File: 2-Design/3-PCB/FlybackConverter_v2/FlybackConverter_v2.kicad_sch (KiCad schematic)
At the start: 52 parts, among them U1 TL431DBV, U2 LM7812_TO220

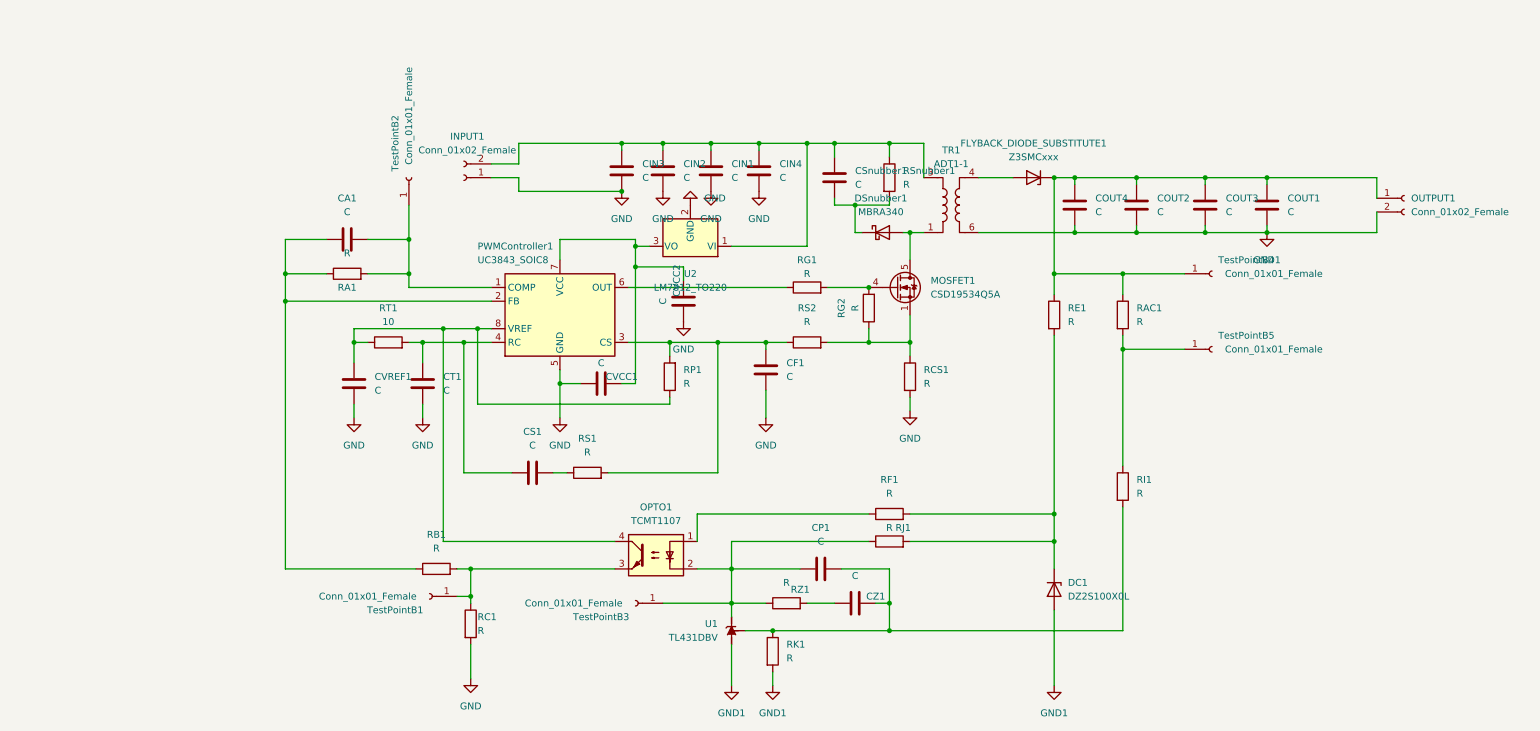
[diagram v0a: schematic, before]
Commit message: FlybackConverter_v2 first placement done, gate loop is too long, positions will be updated blockwise.
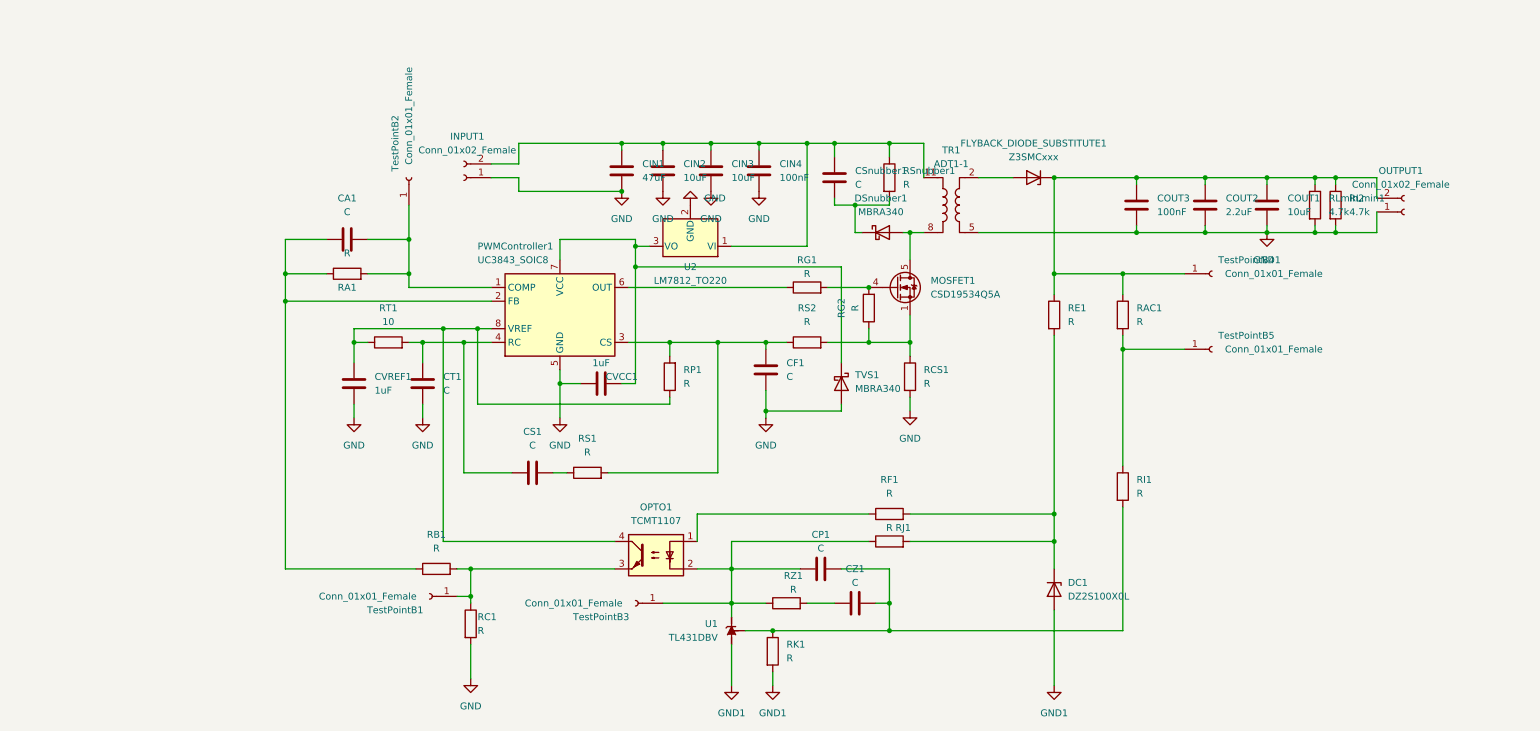
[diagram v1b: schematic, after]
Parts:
- removed COUT4: C, Capacitor_SMD:CP_Elec_10x10.5, symbol Device:C
- removed CVCC2: C, Capacitor_SMD:CP_Elec_8x5.4, symbol Device:C
- added RLmin1, RLmin2: 4.7k, Resistor_SMD:R_1206_3216Metric_Pad1.30x1.75mm_HandSolder, symbol Device:R
- added TVS1: MBRA340, Diode_SMD:D_SMA, symbol Diode:MBRA340
- CIN1: renamed from CIN3; value C -> 47uF; footprint Capacitor_SMD:CP_Elec_10x10.5 -> Capacitor_SMD:CP_Elec_6.3x7.7
- CIN2, COUT1: value C -> 10uF; footprint Capacitor_SMD:CP_Elec_10x10.5 -> Capacitor_SMD:C_1206_3216Metric_Pad1.33x1.80mm_HandSolder
- CIN3: renamed from CIN1; value C -> 10uF; footprint Capacitor_SMD:CP_Elec_10x10.5 -> Capacitor_SMD:C_1206_3216Metric_Pad1.33x1.80mm_HandSolder
- CIN4: value C -> 100nF; footprint Capacitor_SMD:CP_Elec_10x10.5 -> Capacitor_SMD:C_1206_3216Metric_Pad1.33x1.80mm_HandSolder
- COUT2: renamed from COUT3; value C -> 2.2uF; footprint Capacitor_SMD:CP_Elec_10x10.5 -> Capacitor_SMD:C_1206_3216Metric_Pad1.33x1.80mm_HandSolder
- COUT3: renamed from COUT2; value C -> 100nF; footprint Capacitor_SMD:CP_Elec_10x10.5 -> Capacitor_SMD:C_1206_3216Metric_Pad1.33x1.80mm_HandSolder
- CVCC1, CVREF1: value C -> 1uF; footprint Capacitor_SMD:C_0805_2012Metric_Pad1.18x1.45mm_HandSolder -> Capacitor_SMD:C_1206_3216Metric_Pad1.33x1.80mm_HandSolder
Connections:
- net GND: now also TVS1.2 (A)
- net GND1: now also OUTPUT1.1 (Pin_1), TR1.5, RLmin1.2, RLmin2.2; no longer OUTPUT1.2 (Pin_2), TR1.6
- net at CIN1.1, CIN2.1, CIN3.1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: now also TR1.11; no longer TR1.3
- net at COUT1.1, COUT2.1, COUT3.1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: now also OUTPUT1.2 (Pin_2), RLmin1.1, RLmin2.1; no longer OUTPUT1.1 (Pin_1)
- net at FLYBACK_DIODE_SUBSTITUTE1.2 (A): now also TR1.2; no longer TR1.4
- net at DSnubber1.2 (A), MOSFET1.5 (D): now also TR1.8; no longer TR1.1
- net at CVCC1.2, PWMController1.7 (VCC), U2.3 (VO): now also TVS1.1 (K)

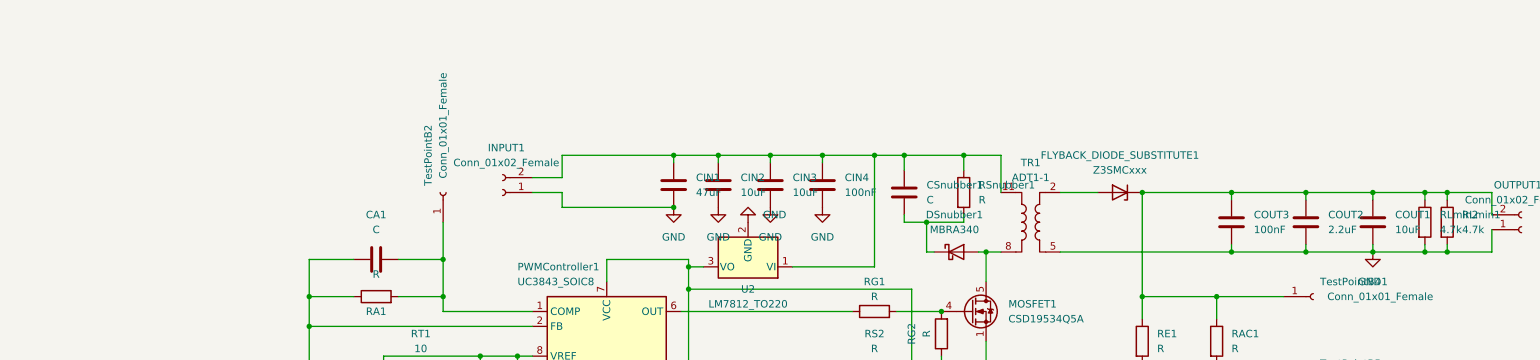
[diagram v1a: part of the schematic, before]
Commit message: FlybackConverter_v2 layout updated. RJ1, 7812, and (maybe) gate driver via problematic.
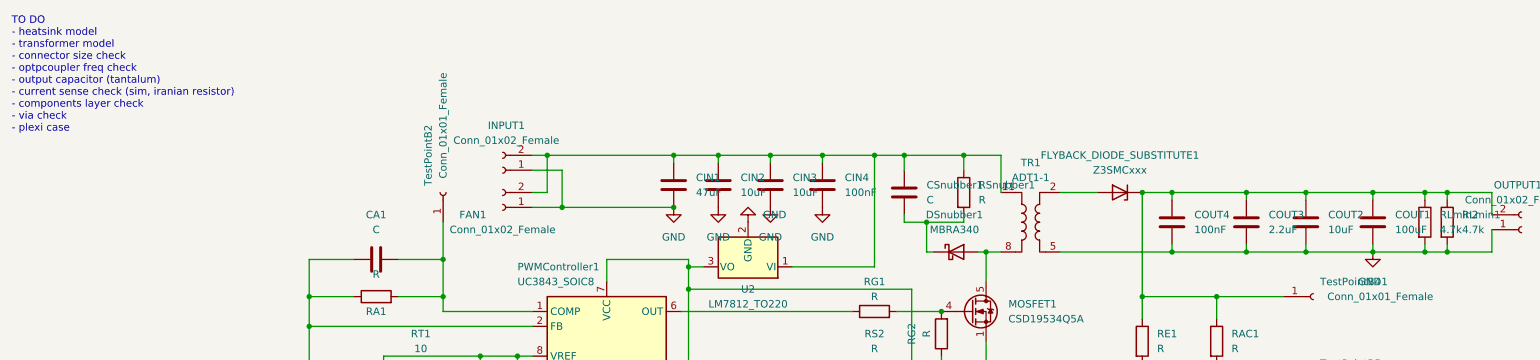
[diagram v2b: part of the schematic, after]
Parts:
- added COUT2: 10uF, Capacitor_SMD:C_1206_3216Metric_Pad1.33x1.80mm_HandSolder, symbol Device:C
- added FAN1: Conn_01x02_Female, Connector_PinHeader_2.54mm:PinHeader_1x02_P2.54mm_Vertical, symbol Connector:Conn_01x02_Female
- COUT1: value 10uF -> 100uF; footprint Capacitor_SMD:C_1206_3216Metric_Pad1.33x1.80mm_HandSolder -> Capacitor_THT:C_Radial_D8.0mm_H11.5mm_P3.50mm
- TVS1: footprint Diode_SMD:D_SMA -> Diode_SMD:D_SOD-123
- U2: footprint Package_TO_SOT_THT:TO-220-3_Vertical -> Package_TO_SOT_SMD:TO-252-2
- renumbered COUT2 to COUT3, COUT3 to COUT4
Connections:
- net GND: now also FAN1.1 (Pin_1)
- net GND1: now also COUT2.2
- net at CIN1.1, CIN2.1, CIN3.1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: now also FAN1.2 (Pin_2)
- net at COUT1.1, COUT3.1, COUT4.1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: now also COUT2.1
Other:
- note added: "TO DO - heatsink model - transformer model - connector size check - optpcoupler freq check - output capacitor (tantalum) - current sense check (sim, iranian resistor) - components layer check - via check - plexi case"
- moved on the sheet: COUT3, COUT4, INPUT1

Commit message: Small updates on schematic and layout.
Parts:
- COUT1: value 100uF -> 47uF; footprint Capacitor_THT:C_Radial_D8.0mm_H11.5mm_P3.50mm -> Capacitor_SMD:CP_Elec_10x12.6
- COUT2: value 10uF -> 2.2uF; footprint Capacitor_SMD:C_1206_3216Metric_Pad1.33x1.80mm_HandSolder -> Capacitor_SMD:C_1210_3225Metric_Pad1.33x2.70mm_HandSolder
- COUT3, COUT4: footprint Capacitor_SMD:C_1206_3216Metric_Pad1.33x1.80mm_HandSolder -> Capacitor_SMD:C_1210_3225Metric_Pad1.33x2.70mm_HandSolder
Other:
- note added: "TO DO - heatsink model - transformer model - connector size check - optpcoupler freq check - current sense check (sim, iranian resistor) - components layer check - via check - plexi case"
- note removed: "TO DO - heatsink model - transformer model - connector size check - optpcoupler freq check - output capacitor (tantalum) - current sense check (sim, iranian resistor) - components layer check - via check - plexi case"
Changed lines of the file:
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@@
     (stroke (width 0) (type default) (color 0 0 0 0))
   )
-  (text "TO DO\n- heatsink model\n- transformer model\n- connector size check\n- optpcoupler freq check\n- output capacitor (tantalum)\n- current sense check (sim, iranian resistor)\n- components layer check\n- via check\n- plexi case\n"
+  (text "TO DO\n- heatsink model\n- transformer model\n- connector size check\n- optpcoupler freq check\n- current sense check (sim, iranian resistor)\n- components layer check\n- via check\n- plexi case\n"
     (at 13.97 34.29 0)
     (effects (font (size 1.27 1.27)) (justify left bottom))
@@
       (effects (font (size 1.27 1.27)) (justify left))
     )
-    (property "Footprint" "Capacitor_SMD:C_1206_3216Metric_Pad1.33x1.80mm_HandSolder" (id 2) (at 213.0552 53.34 0)
+    (property "Footprint" "Capacitor_SMD:C_1210_3225Metric_Pad1.33x2.70mm_HandSolder" (id 2) (at 213.0552 53.34 0)
       (effects (font (size 1.27 1.27)) hide)
     )
@@
       (effects (font (size 1.27 1.27)) (justify left))
     )
-    (property "Footprint" "Capacitor_SMD:C_1206_3216Metric_Pad1.33x1.80mm_HandSolder" (id 2) (at 225.7552 53.34 0)
+    (property "Footprint" "Capacitor_SMD:C_1210_3225Metric_Pad1.33x2.70mm_HandSolder" (id 2) (at 225.7552 53.34 0)
       (effects (font (size 1.27 1.27)) hide)
     )
@@
       (effects (font (size 1.27 1.27)) (justify left))
     )
-    (property "Value" "100uF" (id 1) (at 250.19 50.7999 0)
-      (effects (font (size 1.27 1.27)) (justify left))
-    )
-    (property "Footprint" "Capacitor_THT:C_Radial_D8.0mm_H11.5mm_P3.50mm" (id 2) (at 247.3452 53.34 0)
-      (effects (font (size 1.27 1.27)) hide)
-    )
+    (property "Value" "47uF" (id 1) (at 250.19 50.7999 0)
+      (effects (font (size 1.27 1.27)) (justify left))
+    )
+    (property "Footprint" "Capacitor_SMD:CP_Elec_10x12.6" (id 2) (at 247.3452 53.34 0))
     (property "Datasheet" "~" (id 3) (at 246.38 49.53 0)
       (effects (font (size 1.27 1.27)) hide)
@@
       (effects (font (size 1.27 1.27)) (justify left))
     )
-    (property "Value" "10uF" (id 1) (at 238.76 50.7999 0)
-      (effects (font (size 1.27 1.27)) (justify left))
-    )
-    (property "Footprint" "Capacitor_SMD:C_1206_3216Metric_Pad1.33x1.80mm_HandSolder" (id 2) (at 235.9152 53.34 0)
+    (property "Value" "2.2uF" (id 1) (at 238.76 50.7999 0)
+      (effects (font (size 1.27 1.27)) (justify left))
+    )
+    (property "Footprint" "Capacitor_SMD:C_1210_3225Metric_Pad1.33x2.70mm_HandSolder" (id 2) (at 235.9152 53.34 0)
       (effects (font (size 1.27 1.27)) hide)
     )
@@
     )
     (path "/56efb93a-fc51-4e0f-a22c-c852faba8e99"
-      (reference "COUT1") (unit 1) (value "100uF") (footprint "Capacitor_THT:C_Radial_D8.0mm_H11.5mm_P3.50mm")
+      (reference "COUT1") (unit 1) (value "47uF") (footprint "Capacitor_SMD:CP_Elec_10x12.6")
     )
     (path "/7a9d7d96-fd0a-4884-b61a-e47d6b9e6c56"
-      (reference "COUT2") (unit 1) (value "10uF") (footprint "Capacitor_SMD:C_1206_3216Metric_Pad1.33x1.80mm_HandSolder")
+      (reference "COUT2") (unit 1) (value "2.2uF") (footprint "Capacitor_SMD:C_1210_3225Metric_Pad1.33x2.70mm_HandSolder")
     )
     (path "/109f3c04-2b8e-4fcf-afa5-f222edb3bcb6"
-      (reference "COUT3") (unit 1) (value "2.2uF") (footprint "Capacitor_SMD:C_1206_3216Metric_Pad1.33x1.80mm_HandSolder")
+      (reference "COUT3") (unit 1) (value "2.2uF") (footprint "Capacitor_SMD:C_1210_3225Metric_Pad1.33x2.70mm_HandSolder")
     )
     (path "/0cf29486-8fa5-4a10-bf76-e7b4bee90f2f"
-      (reference "COUT4") (unit 1) (value "100nF") (footprint "Capacitor_SMD:C_1206_3216Metric_Pad1.33x1.80mm_HandSolder")
+      (reference "COUT4") (unit 1) (value "100nF") (footprint "Capacitor_SMD:C_1210_3225Metric_Pad1.33x2.70mm_HandSolder")
     )
     (path "/ddadd4ff-ba23-4d15-a321-847b0478405c"
